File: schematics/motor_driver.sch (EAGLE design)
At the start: 15 parts

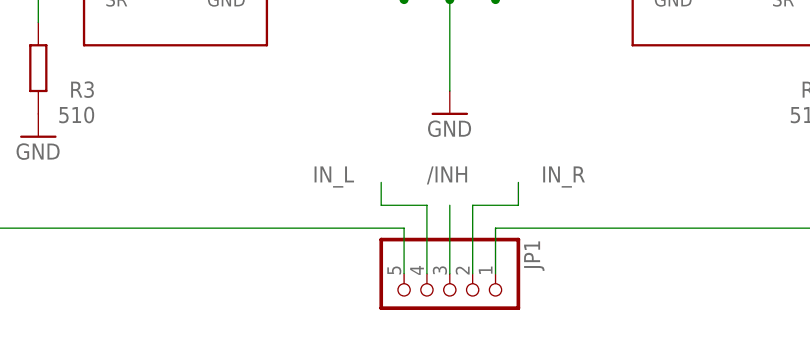
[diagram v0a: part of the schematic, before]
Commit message: Added a common ground for the driver.
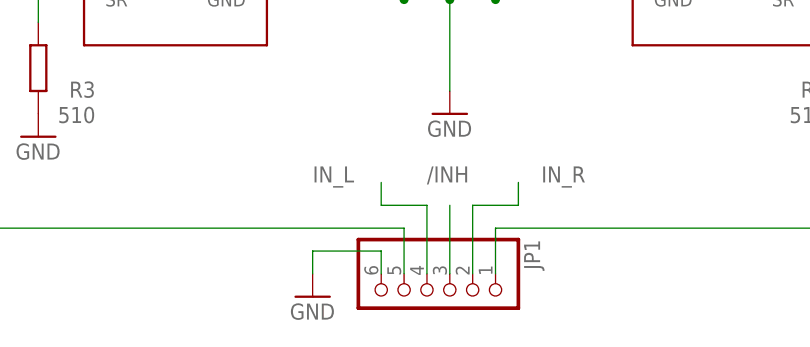
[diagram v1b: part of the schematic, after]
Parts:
- JP1: device pinhead:PINHD-1X5 -> pinhead:PINHD-1X6
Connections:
- net GND: now also JP1.6
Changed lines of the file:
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@@
 <part name="IN_V" library="con-wago-500" deviceset="W237-102" device=""/>
 <part name="M" library="con-wago-500" deviceset="W237-102" device=""/>
-<part name="JP1" library="pinhead" deviceset="PINHD-1X5" device=""/>
 <part name="GND1" library="supply1" deviceset="GND" device=""/>
 <part name="GND2" library="supply1" deviceset="GND" device=""/>
@@
 <part name="GND5" library="supply1" deviceset="GND" device=""/>
 <part name="GND6" library="supply1" deviceset="GND" device=""/>
+<part name="JP1" library="pinhead" deviceset="PINHD-1X6" device=""/>
+<part name="GND7" library="supply1" deviceset="GND" device=""/>
 </parts>
 <sheets>
@@
 <attribute name="NAME" x="68.58" y="69.469" size="1.778" layer="95" rot="R180"/>
 </instance>
-<instance part="JP1" gate="A" x="55.88" y="30.48" rot="R270"/>
 <instance part="GND1" gate="1" x="10.16" y="48.26"/>
 <instance part="GND2" gate="1" x="0" y="48.26"/>
@@
 <instance part="GND5" gate="1" x="101.6" y="48.26"/>
 <instance part="GND6" gate="1" x="111.76" y="48.26"/>
+<instance part="JP1" gate="A" x="53.34" y="30.48" rot="R270"/>
+<instance part="GND7" gate="1" x="40.64" y="30.48"/>
 </instances>
 <busses>
@@
 <pinref part="GND6" gate="1" pin="GND"/>
 </segment>
+<segment>
+<pinref part="JP1" gate="A" pin="6"/>
+<wire x1="48.26" y1="33.02" x2="48.26" y2="35.56" width="0.1524" layer="91"/>
+<wire x1="48.26" y1="35.56" x2="40.64" y2="35.56" width="0.1524" layer="91"/>
+<wire x1="40.64" y1="35.56" x2="40.64" y2="33.02" width="0.1524" layer="91"/>
+<pinref part="GND7" gate="1" pin="GND"/>
+</segment>
 </net>
 <net name="/INH" class="0">
@@
 </segment>
 <segment>
-<pinref part="JP1" gate="A" pin="3"/>
 <wire x1="55.88" y1="33.02" x2="55.88" y2="40.64" width="0.1524" layer="91"/>
 <label x="53.34" y="43.18" size="1.778" layer="95"/>
+<pinref part="JP1" gate="A" pin="3"/>
 </segment>
 </net>
@@
 </segment>
 <segment>
-<pinref part="JP1" gate="A" pin="4"/>
 <wire x1="53.34" y1="33.02" x2="53.34" y2="40.64" width="0.1524" layer="91"/>
 <wire x1="53.34" y1="40.64" x2="48.26" y2="40.64" width="0.1524" layer="91"/>
 <wire x1="48.26" y1="40.64" x2="48.26" y2="43.18" width="0.1524" layer="91"/>
 <label x="40.64" y="43.18" size="1.778" layer="95"/>
+<pinref part="JP1" gate="A" pin="4"/>
 </segment>
 </net>
@@
 <wire x1="5.08" y1="68.58" x2="12.7" y2="68.58" width="0.1524" layer="91"/>
 <wire x1="5.08" y1="68.58" x2="5.08" y2="38.1" width="0.1524" layer="91"/>
-<pinref part="JP1" gate="A" pin="5"/>
 <wire x1="5.08" y1="38.1" x2="50.8" y2="38.1" width="0.1524" layer="91"/>
 <wire x1="50.8" y1="38.1" x2="50.8" y2="33.02" width="0.1524" layer="91"/>
 <junction x="5.08" y="68.58"/>
+<pinref part="JP1" gate="A" pin="5"/>
 </segment>
 </net>
@@
 <net name="N$10" class="0">
 <segment>
-<pinref part="JP1" gate="A" pin="1"/>
 <wire x1="60.96" y1="33.02" x2="60.96" y2="38.1" width="0.1524" layer="91"/>
 <wire x1="60.96" y1="38.1" x2="106.68" y2="38.1" width="0.1524" layer="91"/>
@@
 <wire x1="111.76" y1="68.58" x2="106.68" y2="68.58" width="0.1524" layer="91"/>
 <junction x="106.68" y="68.58"/>
+<pinref part="JP1" gate="A" pin="1"/>
 </segment>
 </net>
@@
 </segment>
 <segment>
-<pinref part="JP1" gate="A" pin="2"/>
 <wire x1="58.42" y1="33.02" x2="58.42" y2="40.64" width="0.1524" layer="91"/>
 <wire x1="58.42" y1="40.64" x2="63.5" y2="40.64" width="0.1524" layer="91"/>
 <wire x1="63.5" y1="40.64" x2="63.5" y2="43.18" width="0.1524" layer="91"/>
 <label x="66.04" y="43.18" size="1.778" layer="95"/>
-</segment>
-</net>
+<pinref part="JP1" gate="A" pin="2"/>
+</segment>
+</net>

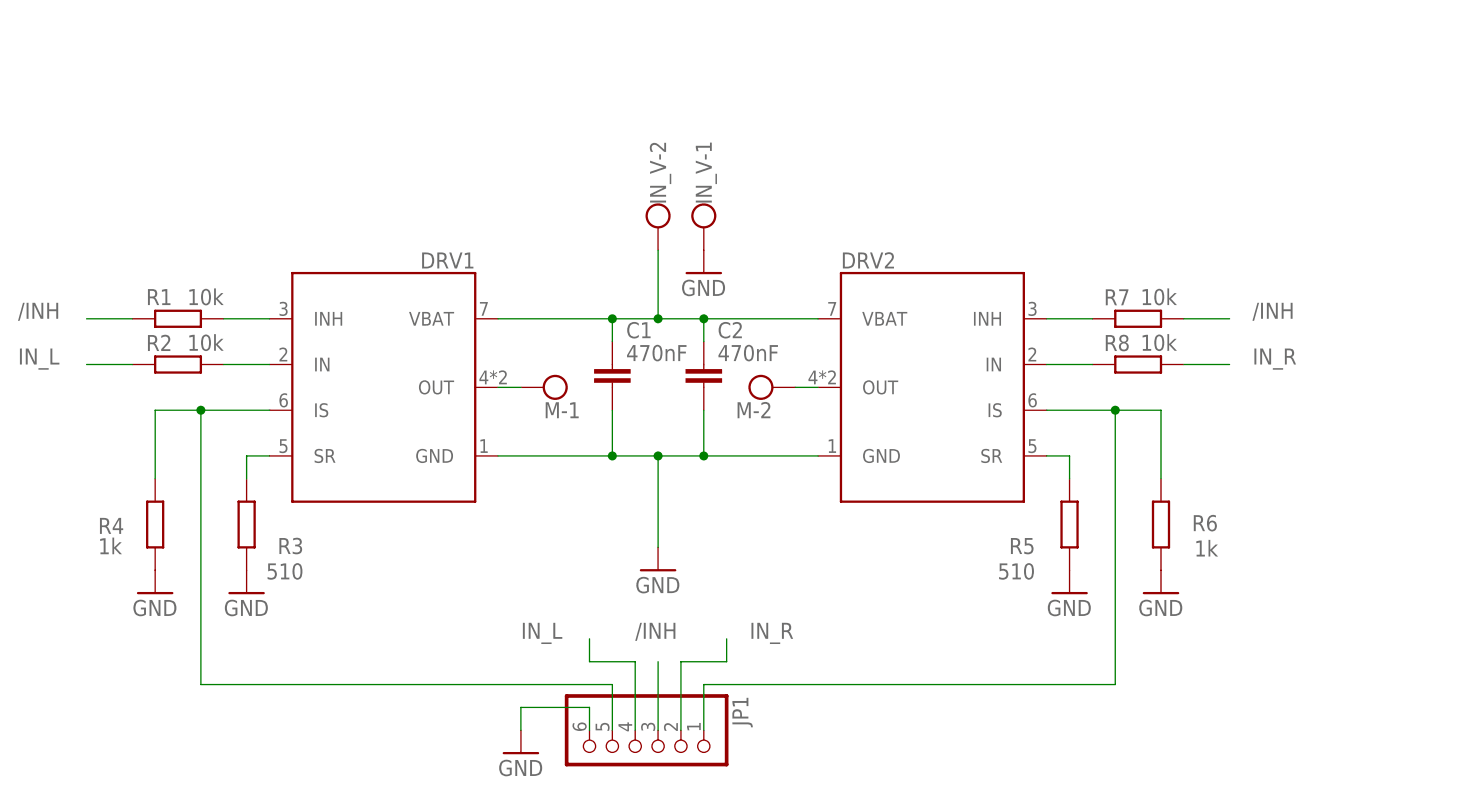
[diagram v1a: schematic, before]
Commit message: Added extra supply caps.
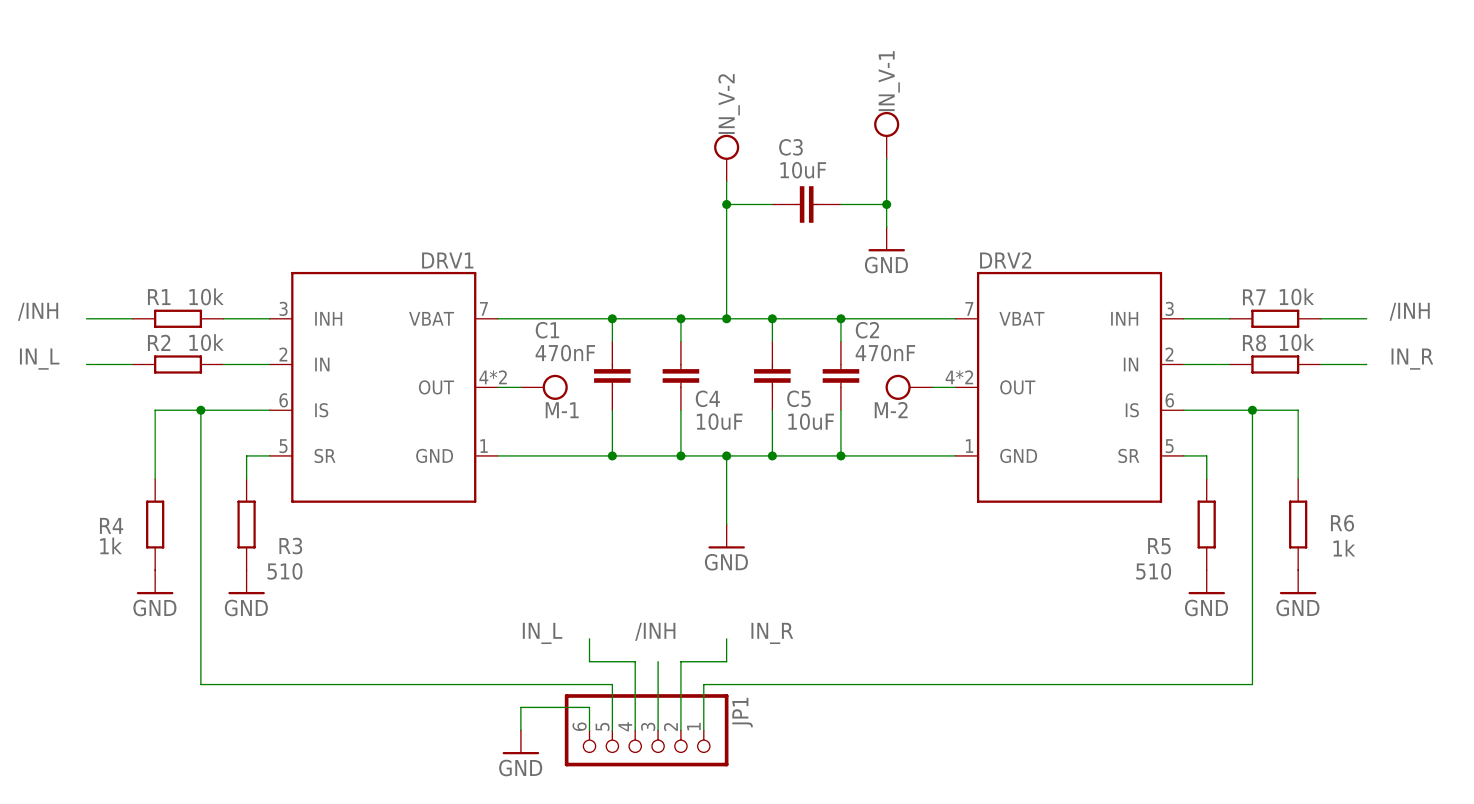
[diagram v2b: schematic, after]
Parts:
- added C3, C4, C5: 10uF, resistor:C-EUC1206
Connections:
- net GND: now also C3.2, C4.2, C5.2
- net VSS: now also C3.1, C4.1, C5.1
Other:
- moved on the sheet: C2, DRV2, IN_V-1, IN_V-2, M-2, R5, R6, R7, R8

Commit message: Added names to unnamed signals.
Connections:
- net N$10 renamed IS_R
- net N$5 renamed IS_L
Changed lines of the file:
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@@
 </segment>
 </net>
-<net name="N$5" class="0">
+<net name="IS_L" class="0">
 <segment>
 <pinref part="R4" gate="G$1" pin="1"/>
@@
 </segment>
 </net>
-<net name="N$10" class="0">
+<net name="IS_R" class="0">
 <segment>
 <wire x1="60.96" y1="33.02" x2="60.96" y2="38.1" width="0.1524" layer="91"/>
